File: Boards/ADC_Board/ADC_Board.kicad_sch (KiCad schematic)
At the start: 84 parts, among them J1 SWD JST PH, J10 I2CC JST, J11 DB9 Microfit, J12 AUX BATT CONN, J2 UART JST, J3 Extras JST, J4 USB_B_Micro, J5 I2CA JST, J6 DB9 Microfit, J7 I2CB JST, J8 CAN1_T, J9 CAN1_T, Q1 DMP6023LFG, U1 STM32G0B1RCTx, U2 TCAN1046, U3 AZ1117C-3.3, U4 AZ1117C-5.0, Y1 8MHz

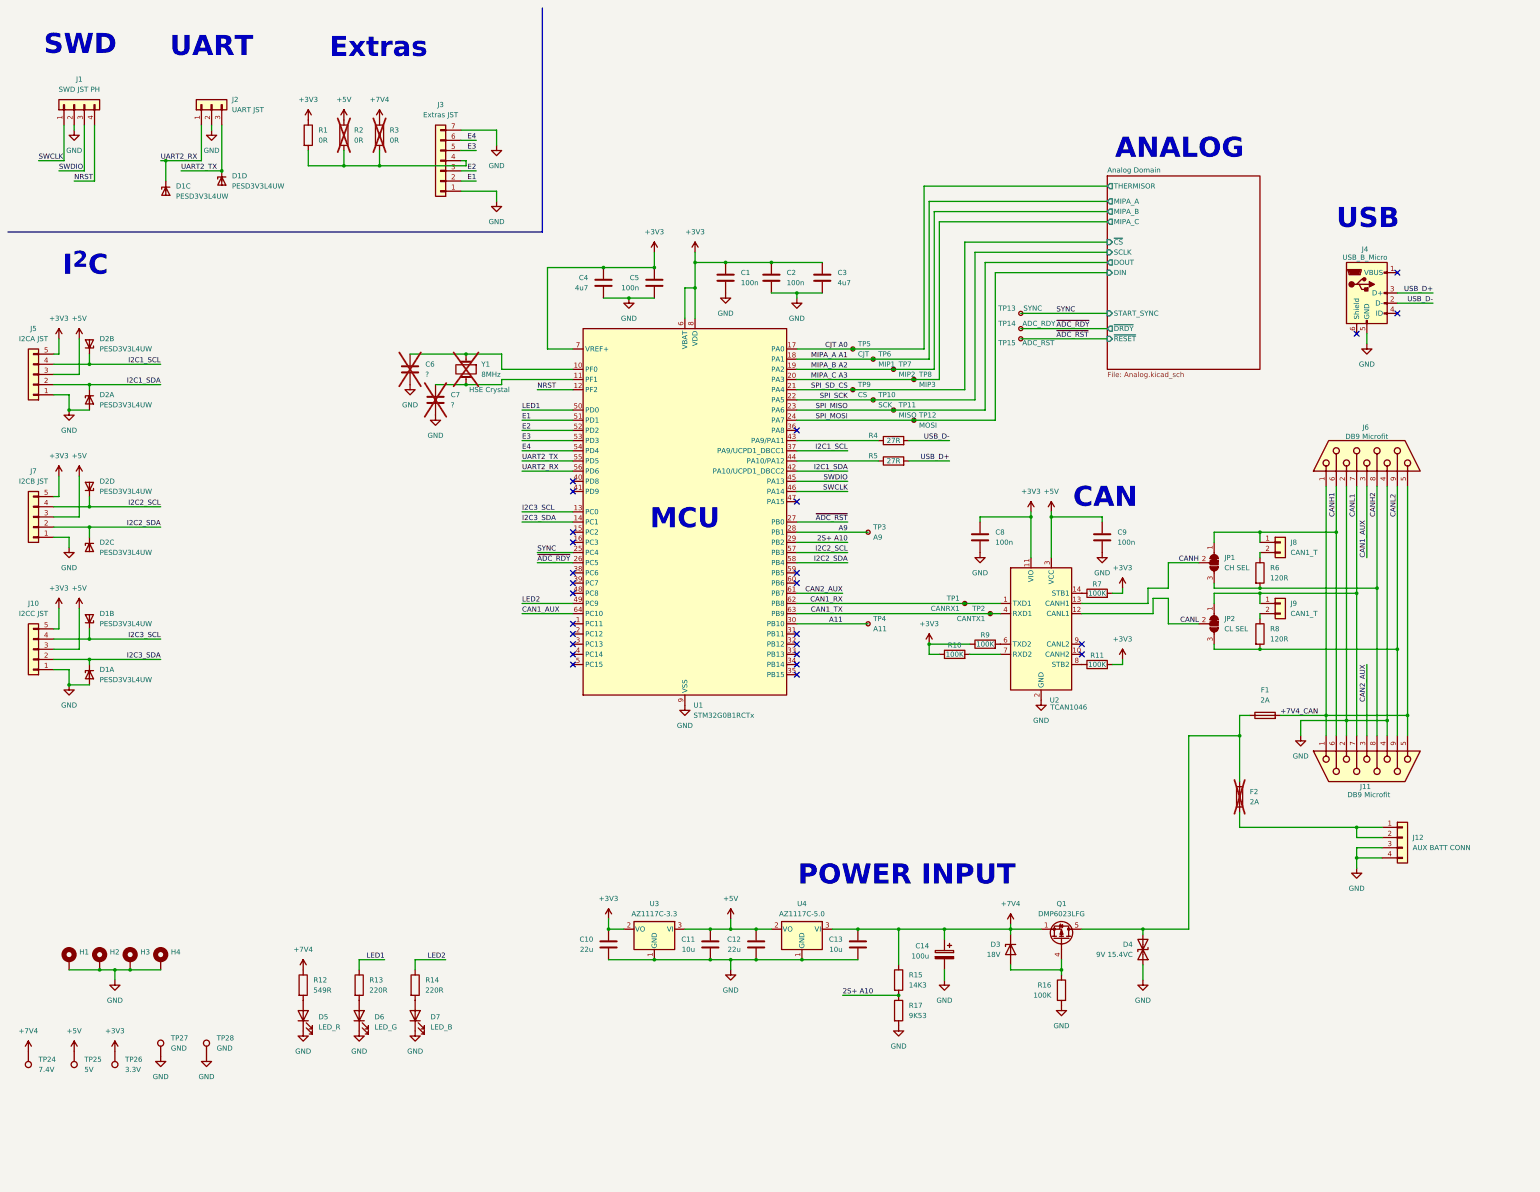
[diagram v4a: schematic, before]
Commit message: Servo nearing completion and ADC 50% layed out
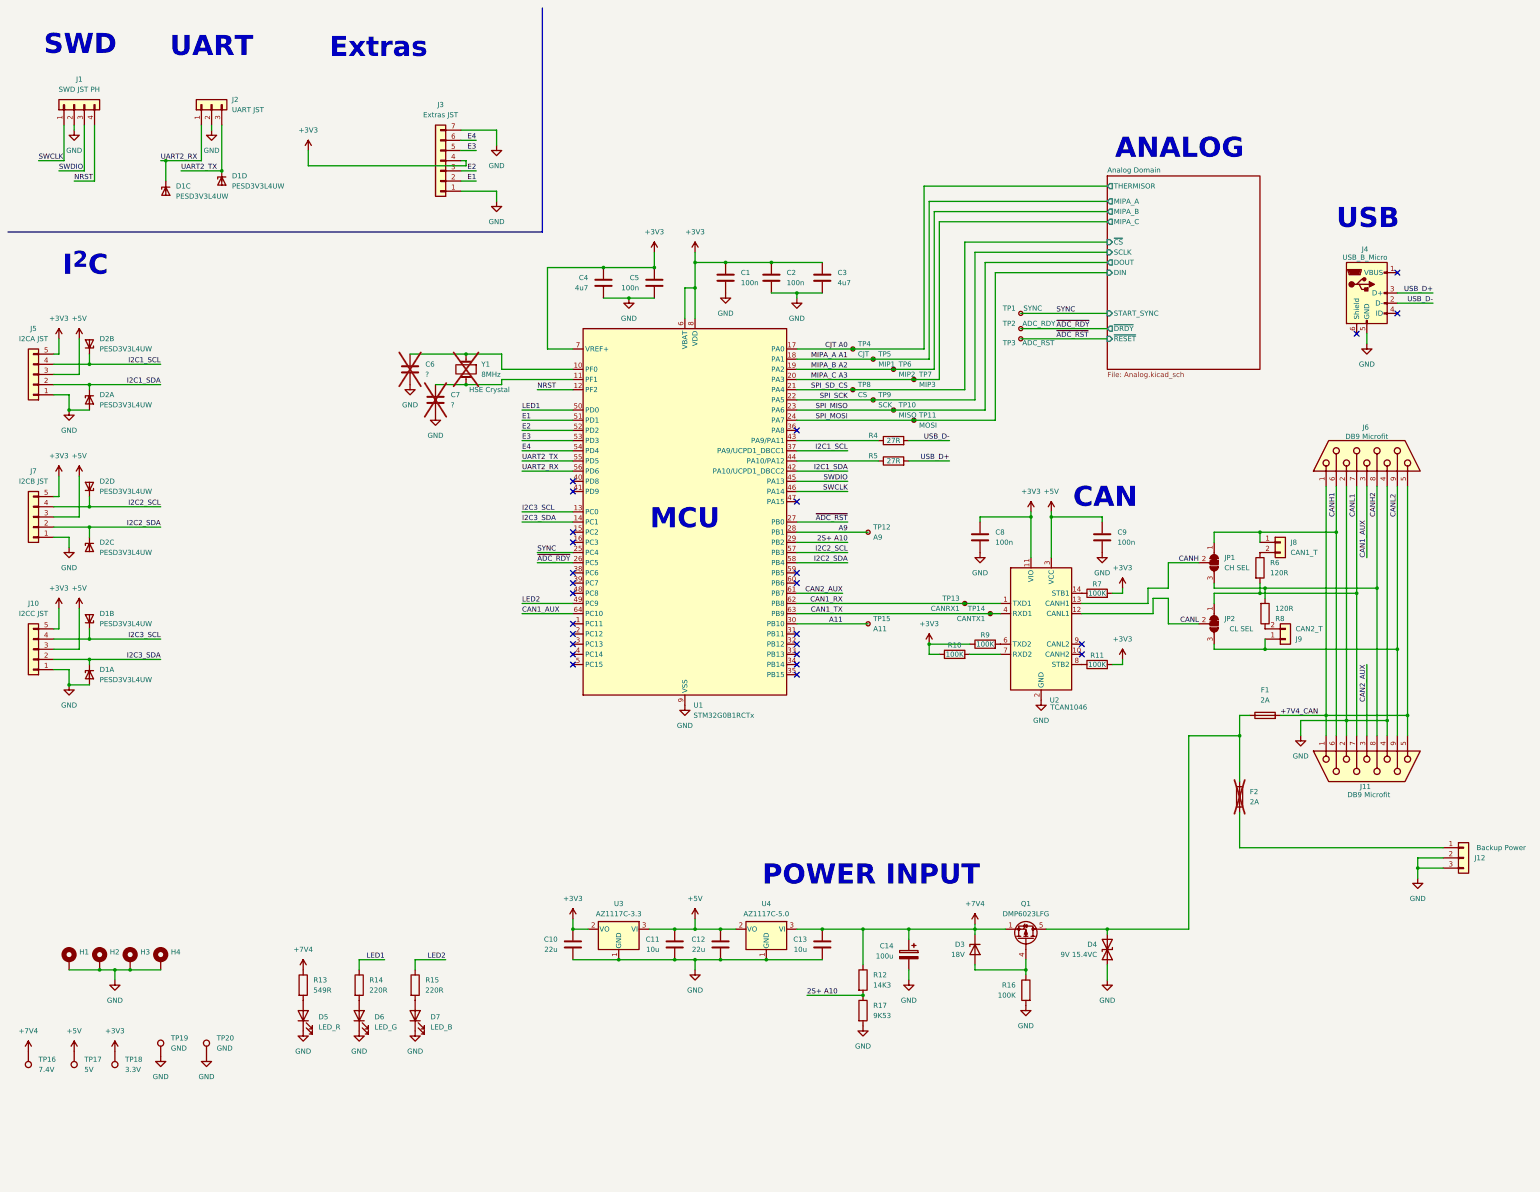
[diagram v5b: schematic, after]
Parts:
- removed J12: AUX BATT CONN, Connector_JST:JST_PH_B4B-PH-K_1x04_P2.00mm_Vertical, symbol Connector_Generic:Conn_01x04
- removed R1, R2, R3: 0R, Resistor_SMD:R_0603_1608Metric, symbol Device:R
- added J12: Backup Power, Connector_Molex:Molex_Micro-Fit_3.0_43650-0315_1x03_P3.00mm_Vertical, symbol Connector_Generic:Conn_01x03
- J11, J6: footprint Connector_Molex:Molex_Micro-Fit_3.0_43045-1012_2x05_P3.00mm_Vertical -> Connector_Dsub:DSUB-9_Pins_Horizontal_P2.77x2.84mm_EdgePinOffset7.70mm_Housed_MountingHolesOffset9.12mm
- J9: value CAN1_T -> CAN2_T
- renumbered R15 to R12, R12 to R13, R13 to R14, R14 to R15, TP13 to TP1, TP11 to TP10, TP12 to TP11, TP3 to TP12, TP1 to TP13, TP2 to TP14, TP4 to TP15, TP24 to TP16, TP25 to TP17, TP26 to TP18, TP27 to TP19, TP14 to TP2, TP28 to TP20, TP15 to TP3, TP5 to TP4, TP6 to TP5, TP7 to TP6, TP8 to TP7, TP9 to TP8, TP10 to TP9
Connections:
- net +3V3: now also J3.4 (Pin_4)
- net CANH2: now also R8.2; no longer R6.2
- net CANL1: now also R6.2; no longer J9.1 (Pin_1)
- net CANL2: now also J9.1 (Pin_1); no longer R8.2
- net GND: now also J12.2 (Pin_2), J12.3 (Pin_3)
- net at F2.1: now also J12.1 (Pin_1)
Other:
- company: (none) -> Hybrid Test Stand
- title: (none) -> ADC ECU Board
- moved on the sheet: C10, C11, C12, C13, C14, D3, D4, J9, Q1, R12, R16, R17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

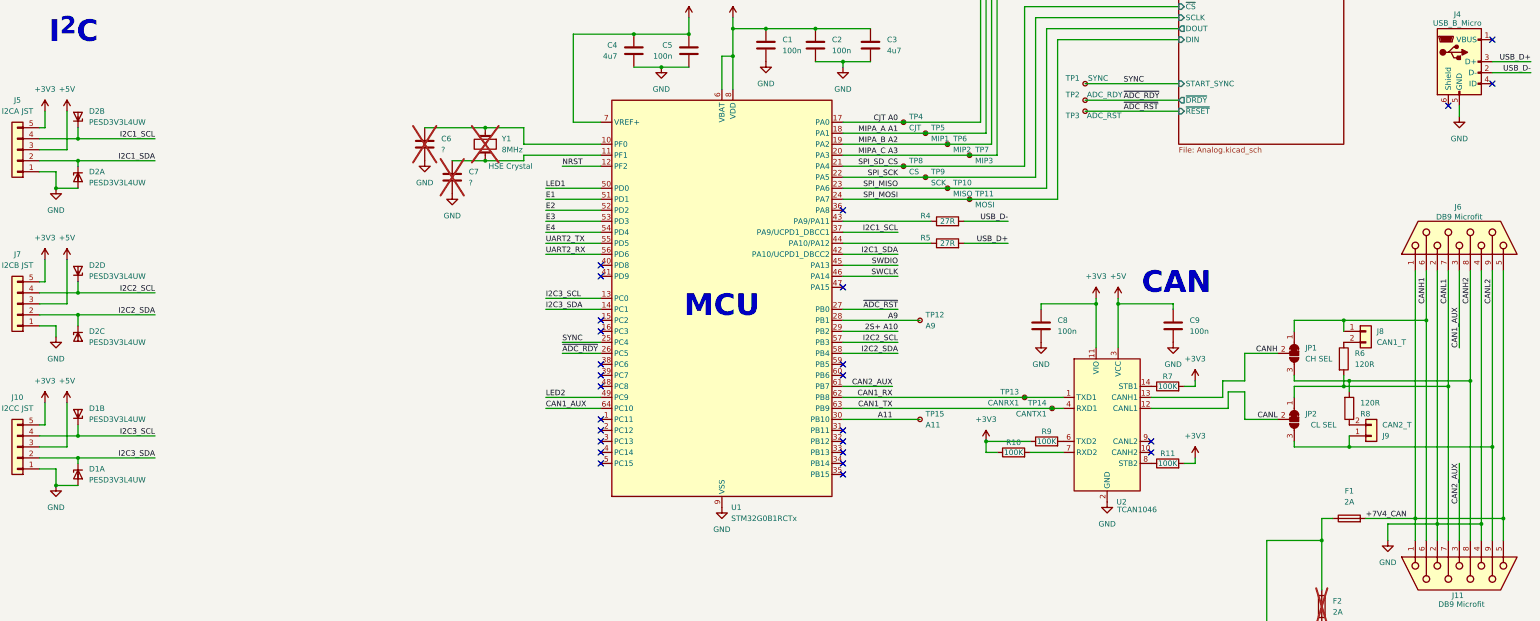
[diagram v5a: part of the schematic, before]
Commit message: Nearing complete layout on both boards
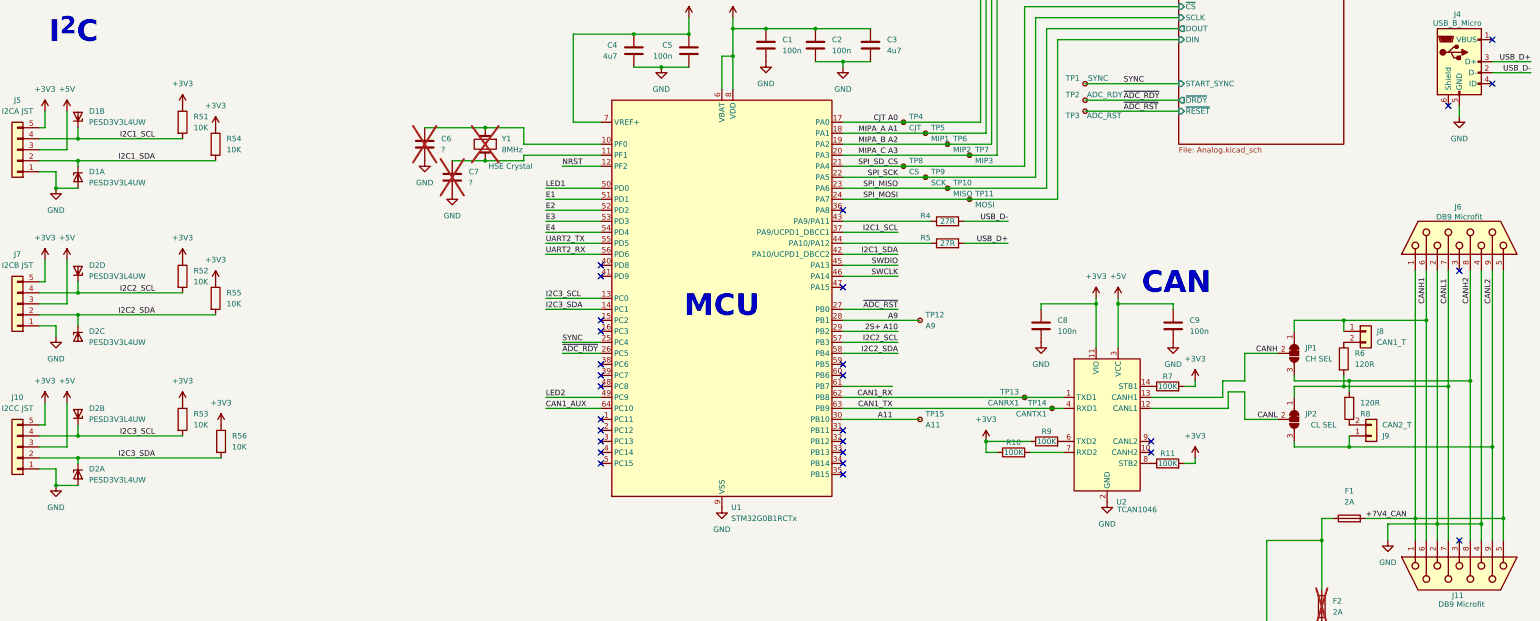
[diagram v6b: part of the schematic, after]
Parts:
- added R51, R52, R53, R54, R55, R56: 10K, Resistor_SMD:R_0603_1608Metric, symbol Device:R
- TP1, TP10, TP11, TP12, TP13, TP14, TP15, TP16, TP17, TP18, TP2, TP3, TP4, TP5, TP6, TP7, TP8, TP9: footprint TestPoint:TestPoint_Pad_1.5x1.5mm -> TestPoint:TestPoint_Pad_D1.0mm
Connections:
- net +3V3: now also R51.1, R52.1, R53.1, R54.1, R55.1, R56.1
- net CAN1_AUX: no longer J6.3
- net I2C1_SCL: now also D1.3 (K2), R51.2; no longer D2.3 (K2)
- net I2C1_SDA: now also D1.1 (K1), R54.2; no longer D2.1 (K1)
- net I2C2_SCL: now also R52.2
- net I2C2_SDA: now also R55.2
- net I2C3_SCL: now also D2.3 (K2), R53.2; no longer D1.3 (K2)
- net I2C3_SDA: now also D2.1 (K1), R56.2; no longer D1.1 (K1)
- net CAN2_AUX: no longer names the net of U1.61 (PB7)
- net CAN2_AUX: no longer J11.3
- no-connect marks 26 -> 28

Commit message: Completed with manufacturing files
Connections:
- net CAN1_AUX: no longer names the net of U1.64 (PC10)
- no-connect marks 28 -> 30
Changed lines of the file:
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@@
 	)
 	(no_connect
+		(at 209.55 158.75)
+	)
+	(no_connect
 		(at 209.55 168.91)
 	)
 	(no_connect
+		(at 153.67 163.83)
+	)
+	(no_connect
 		(at 153.67 171.45)
 	)
@@
 	(wire
 		(pts
-			(xy 140.97 163.83) (xy 153.67 163.83)
-		)
-		(stroke
-			(width 0)
-			(type default)
-		)
-	)
-	(wire
-		(pts
 			(xy 52.07 50.8) (xy 52.07 55.88)
 		)
@@
 	(wire
 		(pts
-			(xy 209.55 158.75) (xy 220.98 158.75)
-		)
-		(stroke
-			(width 0)
-			(type default)
-		)
-	)
-	(wire
-		(pts
 			(xy 254 242.57) (xy 261.62 242.57)
 		)
@@
 		)
 	)
-	(label "CAN1_AUX"
-		(at 140.97 163.83 0)
-		(effects
-			(font
-				(size 1.27 1.27)
-			)
-			(justify left bottom)
-		)
-	)

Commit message: Cleaning out code for firmware
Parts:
- J11: MPN 0430451027 -> A-DF 09 A/KG-T2S
- J6: MPN 0430451027 -> A-DS 09 A/KG-T2S
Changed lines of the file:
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@@
 			)
 		)
-		(property "MPN" "0430451027"
+		(property "MPN" "A-DS 09 A/KG-T2S"
 			(at 351.79 124.46 0)
 			(effects
@@
 			)
 		)
-		(property "MPN" "0430451027"
+		(property "MPN" "A-DF 09 A/KG-T2S"
 			(at 351.79 201.93 0)
 			(effects
